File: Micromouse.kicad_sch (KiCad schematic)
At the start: 0 parts

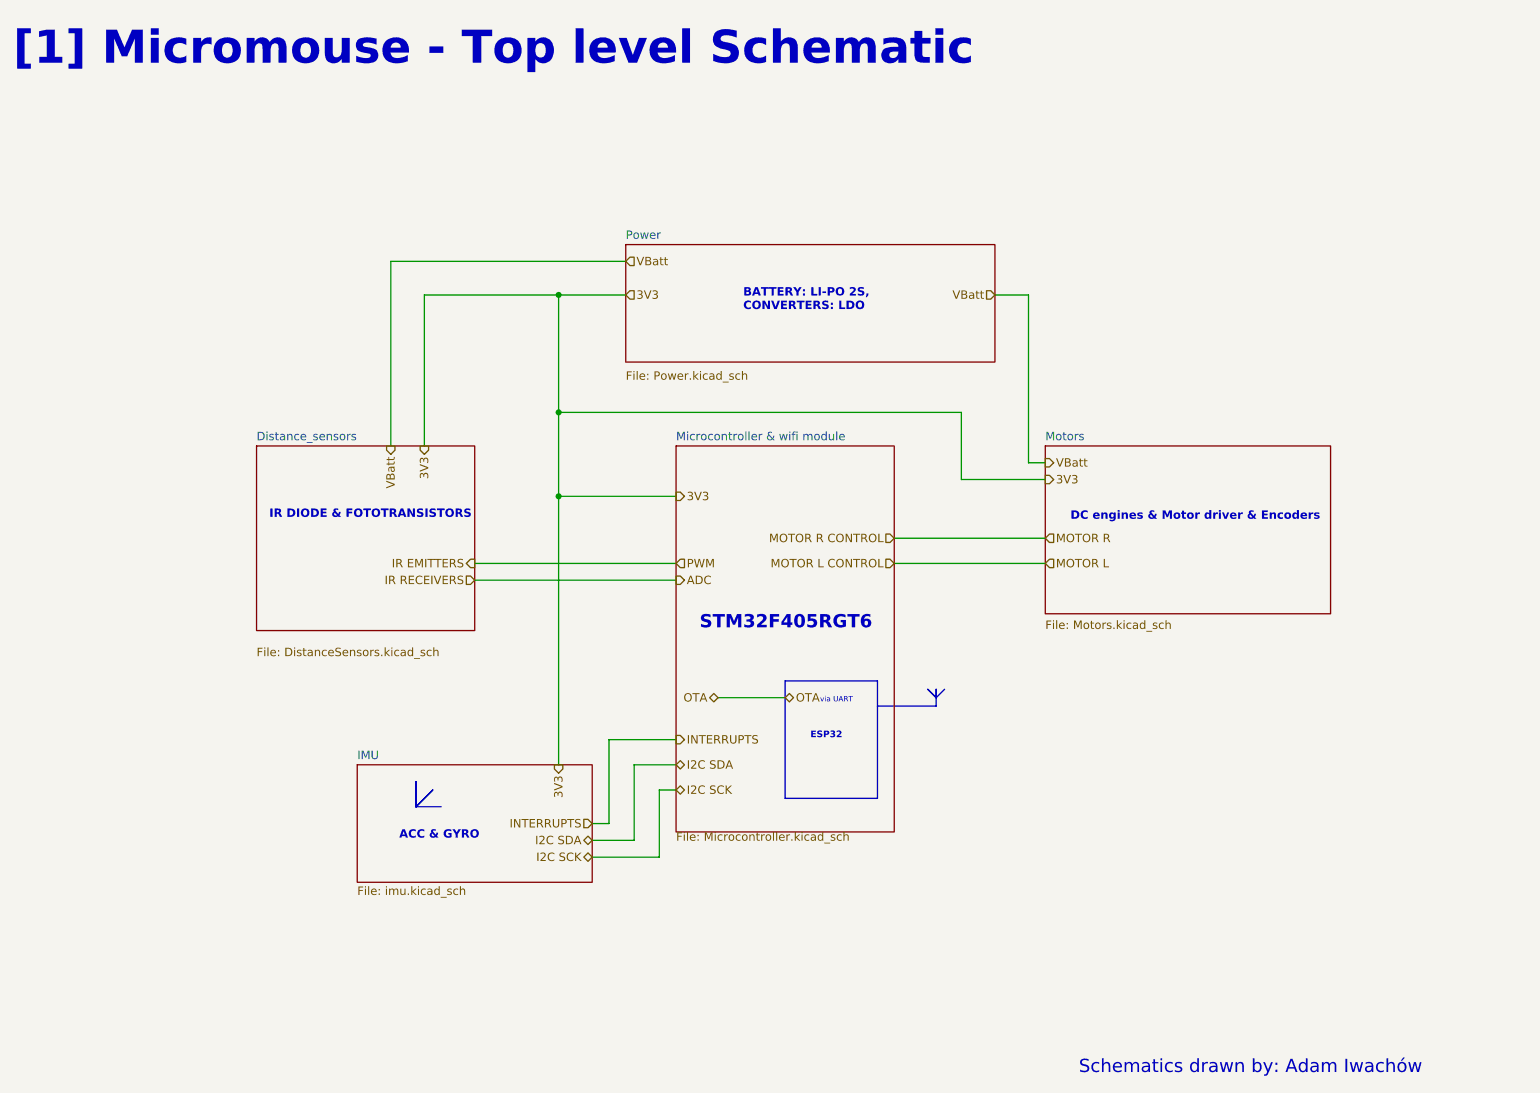
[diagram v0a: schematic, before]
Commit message: improving the hierarchical scheme
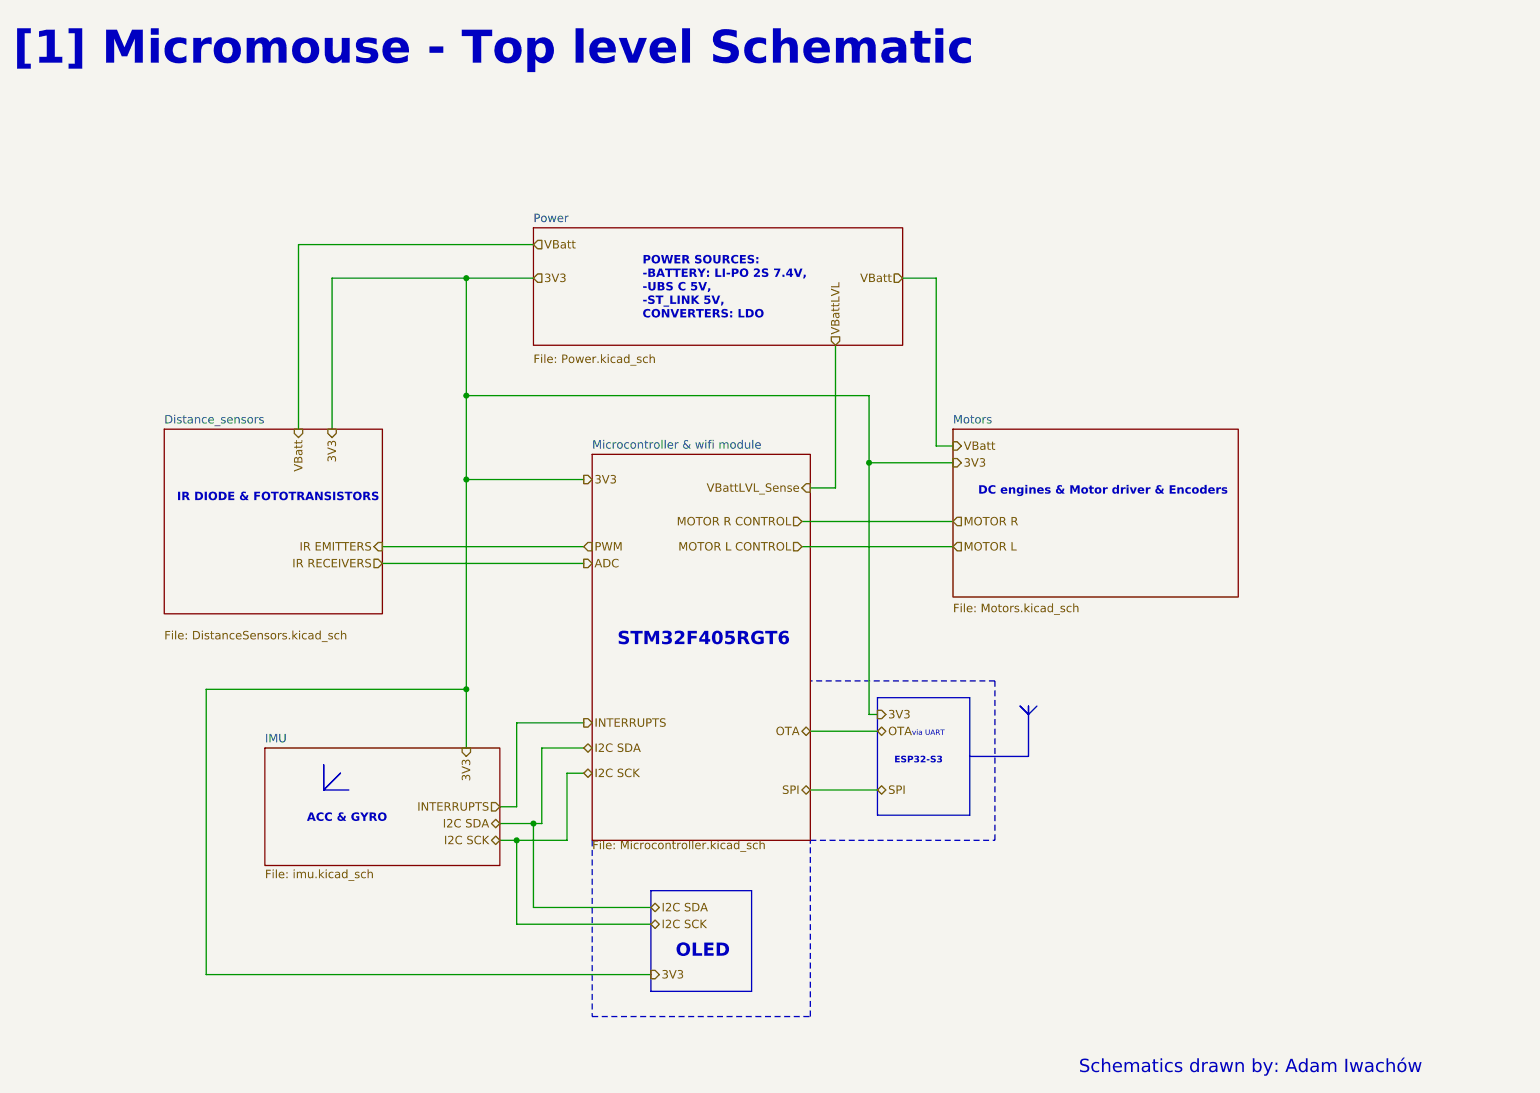
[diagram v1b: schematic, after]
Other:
- note added: "ESP32-S3"
- note added: "OLED"
- note added: "POWER SOURCES: -BATTERY: LI-PO 2S 7.4V, -UBS C 5V, -ST_LINK 5V, CONVERTERS: LDO"
- note removed: "BATTERY: LI-PO 2S, CONVERTERS: LDO"
- note removed: "ESP32"
